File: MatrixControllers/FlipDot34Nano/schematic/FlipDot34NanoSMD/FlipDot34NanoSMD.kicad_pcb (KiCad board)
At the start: 2 copper layers, 67.9 x 46.4 mm, 14 parts, among them J1 FlipDot matrix, J2 I2C bus, J3 Power 24V, SW1 SW_DIP_x03, U1 74HC595D, U2 74HC595D, U3 74HC595D

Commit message: Add ground polygon
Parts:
- moved C1 8.47 mm to (73.0, 66.7), turned to -90 degrees
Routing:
- net GND: track 92.4 -> 23.5 mm, vias 3 -> 1
- net Net-(A1-Pad8): track 52.3 -> 51.2 mm
- net Net-(A1-Pad6): track 20.2 -> 19.3 mm
- added copper zone on F.Cu, net GND

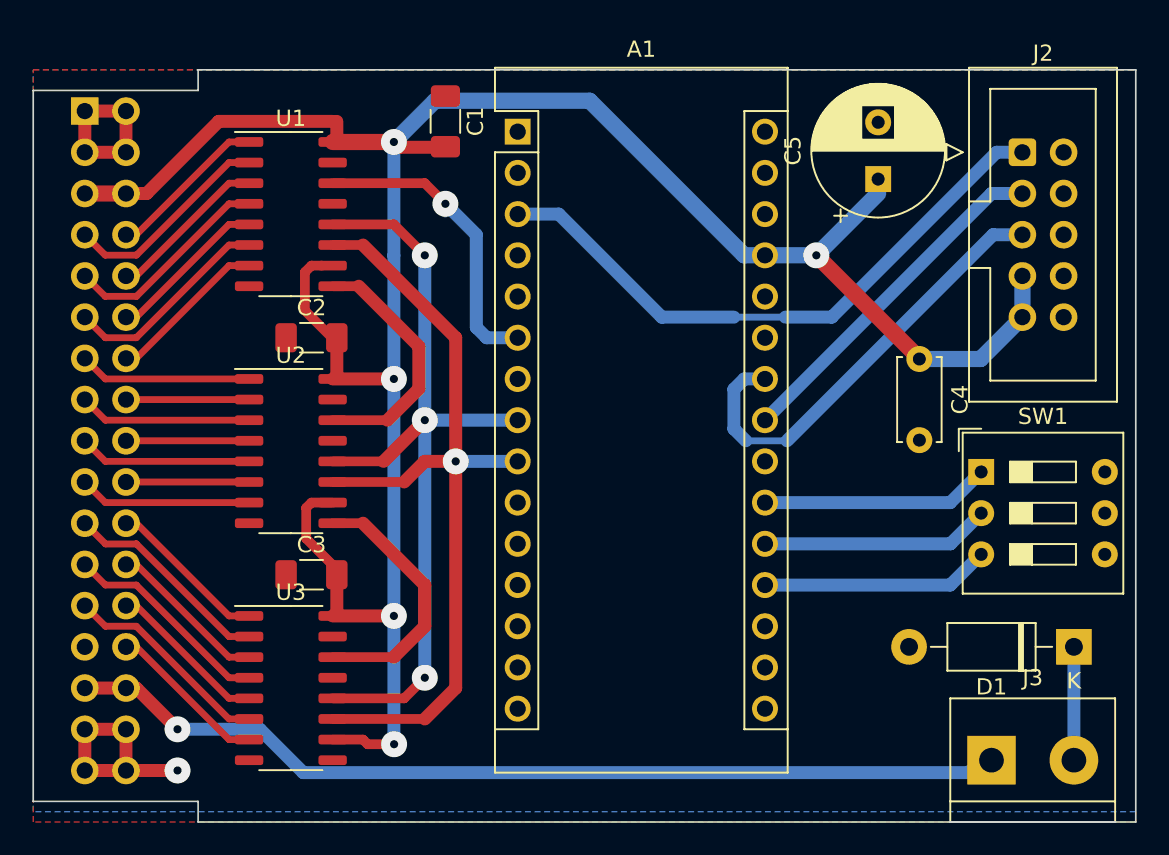
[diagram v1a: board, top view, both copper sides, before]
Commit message: Create MatrixControllerI2C example
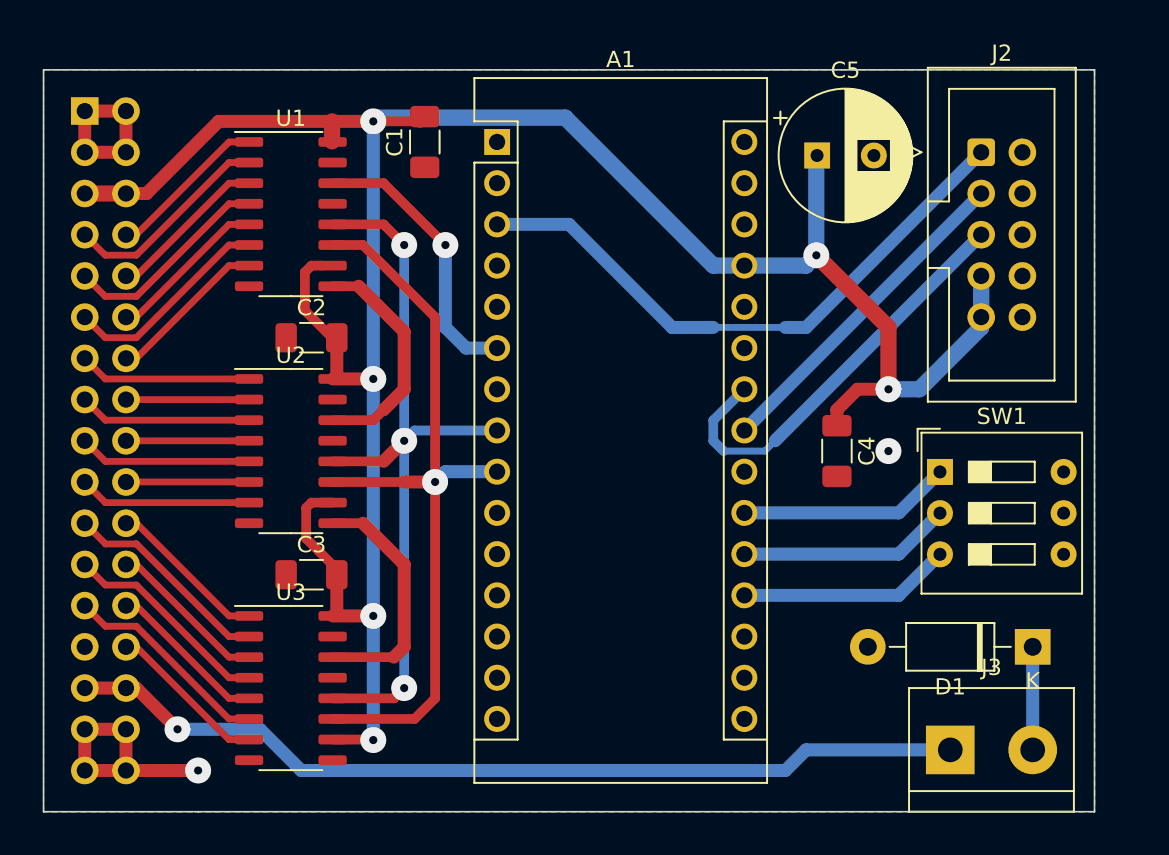
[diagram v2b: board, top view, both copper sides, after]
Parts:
- C4: footprint Capacitor_THT:C_Disc_D5.0mm_W2.5mm_P5.00mm -> Capacitor_SMD:C_1206_3216Metric_Pad1.33x1.80mm_HandSolder
- moved C4 7.62 mm to (97.2, 87.0)
- moved C5 4.03 mm to (95.9, 68.8), turned to 0 degrees
- moved J3 2.62 mm to (104.1, 105.4)
- moved D1 2.54 mm to (109.2, 99.1)
- moved SW1 2.54 mm to (103.5, 88.3)
- moved J2 2.54 mm to (106.0, 68.6)
- moved C1 1.80 mm to (71.8, 67.9), turned to 90 degrees
- moved A1 1.42 mm to (76.2, 67.9)
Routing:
- net Net-(A1-Pad8): track 51.2 -> 47.8 mm
- net Net-(A1-Pad9): track 51.8 -> 48.9 mm
- net Vin: track 148.6 -> 150.8 mm, vias 5 -> 6
- net Net-(A1-Pad6): track 19.3 -> 17.3 mm
- net Net-(J1-Pad29): track 57.5 -> 56.0 mm
- net GND: track 23.5 -> 24.8 mm, vias 1 -> 2
- net Net-(U1-Pad9): track 15.6 -> 14.3 mm
- net SCL: track 27.3 -> 26.3 mm
- net Net-(U2-Pad9): track 16.3 -> 15.2 mm
- net CFG-0: track 14.1 -> 13.1 mm
- net RESET: track 37.9 -> 36.9 mm
- net CFG-1: track 14.1 -> 13.1 mm
- net CFG-2: track 14.1 -> 13.1 mm
- net Net-(D1-Pad1): track 6.98 -> 6.35 mm
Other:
- board size 67.9 x 46.4 mm -> 64.8 x 45.7 mm
